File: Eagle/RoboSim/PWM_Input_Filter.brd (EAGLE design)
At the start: 74.6 x 78.7 mm, 68 parts, among them IC1 LM358, IC2 LM358, IC3 LM358

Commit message: updated op amp part number
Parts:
- IC1, IC2, IC3: value LM358 -> TLV2772
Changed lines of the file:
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@@
 </autorouter>
 <elements>
-<element name="IC1" library="SparkFun-AnalogIC" package="DIP08" value="LM358" x="44.45" y="67.31">
+<element name="IC1" library="SparkFun-AnalogIC" package="DIP08" value="TLV2772" x="44.45" y="67.31">
 <attribute name="PROD_ID" value="IC-09172" x="63.5" y="62.23" size="1.778" layer="27" display="off"/>
 </element>
@@
 <element name="JP1" library="SparkFun-Connectors" package="1X06_LOCK" value="" x="5.08" y="59.69" rot="R90"/>
 <element name="JP2" library="SparkFun-Connectors" package="1X06_LOCK" value="" x="69.85" y="44.45" rot="R270"/>
-<element name="IC2" library="SparkFun-AnalogIC" package="DIP08" value="LM358" x="50.8" y="44.45">
+<element name="IC2" library="SparkFun-AnalogIC" package="DIP08" value="TLV2772" x="50.8" y="44.45">
 <attribute name="PROD_ID" value="IC-09172" x="82.55" y="39.37" size="1.778" layer="27" display="off"/>
 </element>
@@
 <element name="TP4" library="SparkFun-Passives" package="PAD.03X.03" value="TEST-POINT3" x="21.59" y="48.26"/>
 <element name="C8" library="SparkFun-Passives" package="CAP-PTH-SMALL" value="100uF" x="59.69" y="39.37" rot="R180"/>
-<element name="IC3" library="SparkFun-AnalogIC" package="DIP08" value="LM358" x="52.07" y="15.24">
+<element name="IC3" library="SparkFun-AnalogIC" package="DIP08" value="TLV2772" x="52.07" y="15.24">
 <attribute name="PROD_ID" value="IC-09172" x="96.52" y="10.16" size="1.778" layer="27" display="off"/>
 </element>

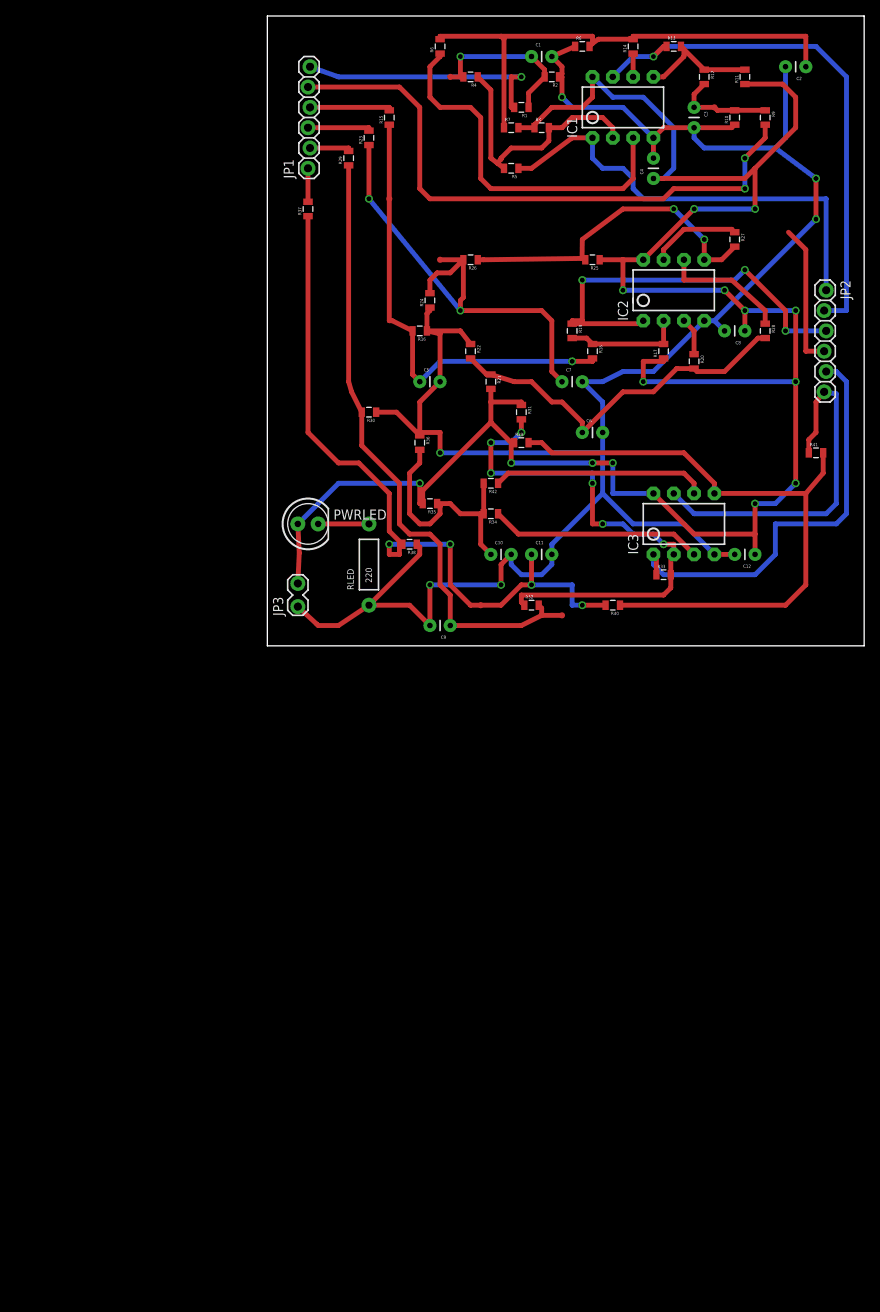
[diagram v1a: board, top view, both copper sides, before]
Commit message: Updated pwm input filter schematic
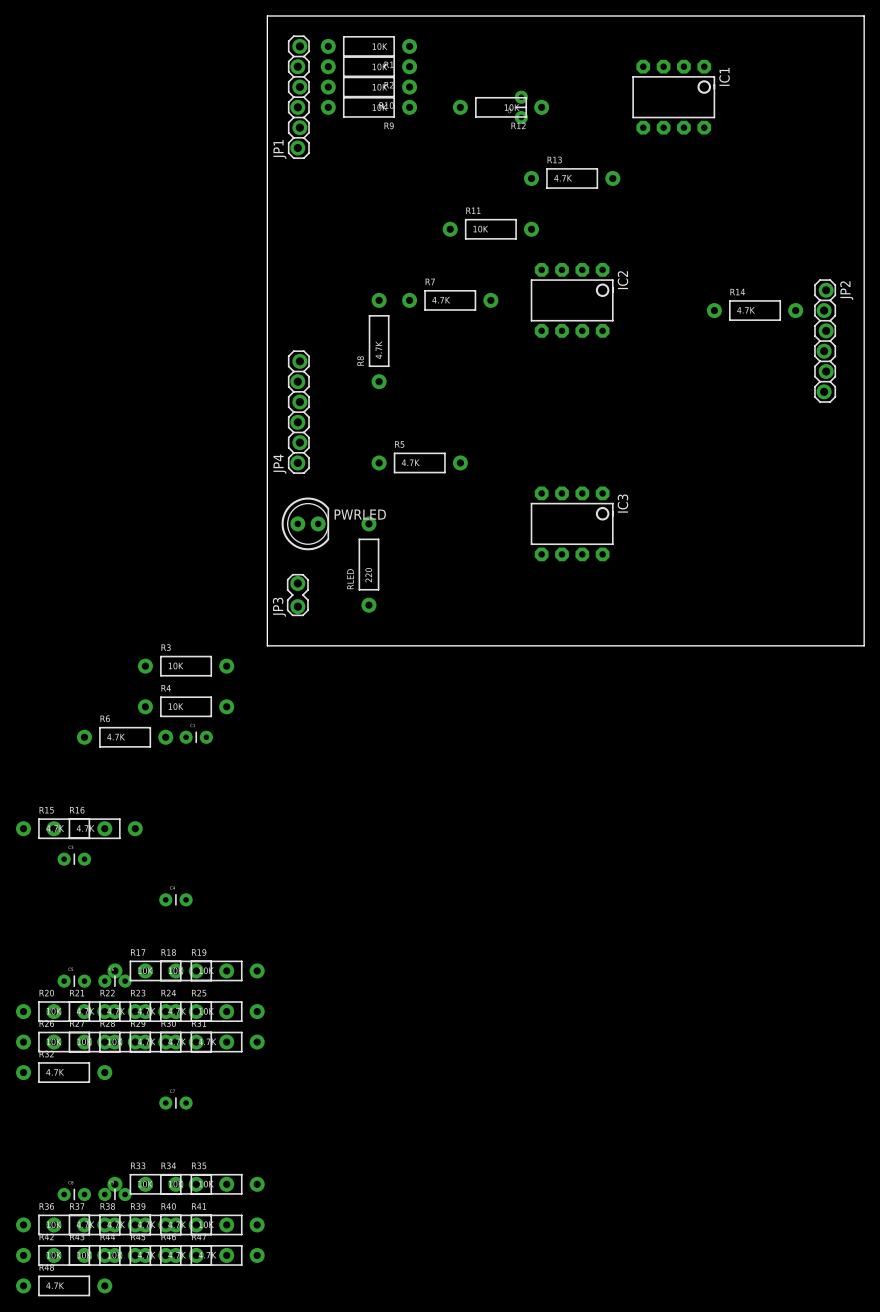
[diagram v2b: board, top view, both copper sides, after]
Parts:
- removed C10, C12: 100uF, SparkFun-Passives:CAP-PTH-SMALL
- removed C11: 0.5uF, SparkFun-Passives:CAP-PTH-SMALL
- removed TP1, TP2, TP3, TP4, TP5, TP6: TEST-POINT3, SparkFun-Passives:PAD.03X.03
- added JP4: (no value), SparkFun-Connectors:1X06_LOCK
- added R43, R44: 10K, SparkFun-Passives:AXIAL-0.4
- added R45, R46, R47, R48: 4.7K, SparkFun-Passives:AXIAL-0.4
- C1, C3, C5, C7, C9: value 0.5uF -> 100uF
- R1, R11, R12, R17, R18, R19, R20, R25, R26, R27, R28, R3, R33, R34, R35, R36, R4, R41, R42, R9: value 80K -> 10K; device SparkFun-Passives:0805 -> SparkFun-Passives:AXIAL-0.4
- R10, R2: value 20K -> 10K; device SparkFun-Passives:0805 -> SparkFun-Passives:AXIAL-0.4
- R13, R14, R15, R21, R22, R23, R29, R31, R32, R37, R39, R40, R5, R6, R7, R8: value 80K -> 4.7K; device SparkFun-Passives:0805 -> SparkFun-Passives:AXIAL-0.4
- R16, R24, R30, R38: value 20K -> 4.7K; device SparkFun-Passives:0805 -> SparkFun-Passives:AXIAL-0.4
- moved C8 137.5 mm to (-25.4, -68.6), turned to 0 degrees
- moved R37 129.8 mm to (-21.6, -72.4), turned to 0 degrees
- moved R27 128.3 mm to (-21.6, -49.5), turned to 0 degrees
- moved C3 122.6 mm to (-25.4, -26.7), turned to 0 degrees
- moved R41 122.2 mm to (-6.35, -72.4)
- moved R28 119.6 mm to (-17.8, -49.5), turned to 0 degrees
- moved R20 113.2 mm to (-25.4, -45.7), turned to 0 degrees
- moved R29 113.1 mm to (-14.0, -49.5), turned to 0 degrees
- moved R23 112.4 mm to (-14.0, -45.7), turned to 0 degrees
- moved R42 110.3 mm to (-25.4, -76.2), turned to 0 degrees
- moved R26 110.2 mm to (-25.4, -49.5), turned to 0 degrees
- moved C4 108.8 mm to (-12.7, -31.8), turned to 0 degrees
- moved R39 107.9 mm to (-14.0, -72.4)
- moved R36 107.4 mm to (-25.4, -72.4), turned to 0 degrees
- moved R25 105.1 mm to (-6.35, -45.7), turned to 0 degrees
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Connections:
- removed net N$4: IC1.1, JP2.1, R5.1
- new net N$18: C6.1, IC2.7, JP2.4, R30.P$2
- new net N$19: JP4.6, R26.P$2
- new net N$23: IC2.3, R17.P$1, R20.P$2, R23.P$2
- new net N$24: R21.P$2, R22.P$1
- new net N$29: R31.P$1, R32.P$2
- new net N$34: JP4.2, R42.P$2
- new net N$35: JP4.1, R41.P$2
- new net N$43: R47.P$1, R48.P$2
- new net N$44: C1.1, IC1.1, JP2.1, R6.P$2
- new net N$6: IC1.2, R1.P$1, R3.P$2, R5.P$1
- net GND: now also R16.P$1, R24.P$1, R32.P$1, R40.P$1, R48.P$1, R8.P$1; no longer C10.2, C11.2, C12.2, R10.1, R16.1, R2.1, R22.1, R24.1, R30.1, R36.1, R38.1, R8.1
- net N$1: now also R1.P$2; no longer R1.2
- net N$10: now also R7.P$1, R8.P$2; no longer IC1.5, R11.2, R12.1, R13.2
- net N$11: now also IC1.5, R10.P$1, R11.P$2, R13.P$1; no longer C2.1, R14.2, R6.2, R7.1, R8.2
- net N$12: now also R12.P$2, R15.P$2, R9.P$1; no longer R14.1
- net N$13: now also C3.1, R14.P$2; no longer R13.1
- net N$14: now also R10.P$2; no longer R15.2
- net N$15: now also R13.P$2, R14.P$1; no longer C5.1, R15.1, R16.2, R18.2, TP3.P$1
- net N$16: now also JP1.1, R17.P$2; no longer IC2.1, JP2.3, R19.1
- net N$17: now also R15.P$1, R16.P$2; no longer IC2.2, R17.2, R18.1, R19.2
- net N$2: now also JP1.2, R18.P$2; no longer C1.1, R1.1, R2.2, R4.2, TP1.P$1
- net N$20: now also JP4.5, R25.P$2; no longer IC2.3, R20.1
- net N$21: now also R9.P$2; no longer R23.2
- net N$22: now also IC2.2, R18.P$1, R19.P$2, R21.P$1; no longer C7.1, R23.1, R24.2, R26.2, TP4.P$1
- net N$25: now also R23.P$1, R24.P$2; no longer IC2.5, R25.2, R26.1, R27.2
- net N$26: now also IC2.5, R26.P$1, R27.P$2, R29.P$1; no longer C6.1, R20.2, R21.1, R22.2, R28.2
- net N$27: now also IC2.6, R25.P$1, R28.P$2, R31.P$2; no longer IC3.1, JP2.5, R33.1
- net N$28: now also R29.P$2, R30.P$1; no longer IC2.6, R28.1
- net N$3: now also C5.1, IC2.1, JP2.3, R22.P$2; no longer IC1.2, R3.2, R4.1, R5.2
- net N$30: now also JP4.4, R34.P$2; no longer IC2.7, JP2.4, R27.1
- net N$31: now also C8.1, IC3.1, JP2.5, R38.P$2; no longer JP1.2, R29.2
- net N$32: now also JP4.3, R33.P$2; no longer C9.1, R29.1, R30.2, R32.2, TP5.P$1
- net N$33: now also C9.1, IC3.7, JP2.6, R46.P$2; no longer IC3.2, R31.2, R32.1, R33.2
- net N$36: now also IC3.2, R34.P$1, R35.P$2, R37.P$1; no longer IC3.3, R34.1
- net N$37: now also IC3.3, R33.P$1, R36.P$2, R39.P$2; no longer JP1.1, R37.2
- net N$38: now also R37.P$2, R38.P$1; no longer C11.1, R37.1, R38.2, R40.2, TP6.P$1
- net N$39: now also R39.P$1, R40.P$2; no longer IC3.5, R39.2, R40.1, R41.2
- net N$40: now also IC3.5, R42.P$1, R43.P$2, R45.P$1; no longer C10.1, R34.2, R35.1, R36.2, R42.2
- net N$41: now also R41.P$1, R44.P$2, R47.P$2; no longer R42.1
- net N$42: now also R45.P$2, R46.P$1; no longer IC3.7, JP2.6, R41.1
- net N$7: now also R2.P$1, R4.P$2, R7.P$2; no longer R6.1
- net N$8: now also R2.P$2; no longer R9.2
- net N$9: now also R5.P$2, R6.P$1; no longer C3.1, R10.2, R12.2, R9.1, TP2.P$1
- net VCC: now also C2.1, C7.1, R11.P$1, R12.P$1, R19.P$1, R20.P$1, R27.P$1, R28.P$1, R3.P$1, R35.P$1, R36.P$1, R4.P$1, R43.P$1, R44.P$1; no longer C12.1, C8.1, R11.1, R17.1, R21.2, R25.1, R3.1, R31.1, R35.2, R39.1, R7.2
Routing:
- net VCC: track 273.1 -> 0.00 mm, vias 14 -> 0
- net GND: track 267.9 -> 0.00 mm, vias 6 -> 0
- net N$38: track 92.1 -> 0.00 mm, vias 4 -> 0
- net N$32: track 79.6 -> 0.00 mm
- net N$39: track 79.6 -> 0.00 mm
- net N$8: track 75.9 -> 0.00 mm, vias 2 -> 0
- net N$13: track 66.5 -> 0.00 mm, vias 1 -> 0
- net N$33: track 66.1 -> 0.00 mm, vias 6 -> 0
- net N$11: track 63.4 -> 0.00 mm
- net N$22: track 61.2 -> 0.00 mm, vias 2 -> 0
- net N$15: track 57.4 -> 0.00 mm, vias 1 -> 0
- net N$4: track 56.6 -> 0.00 mm
- net N$27: track 53.6 -> 0.00 mm
- net N$16: track 51.4 -> 0.00 mm, vias 3 -> 0
- net N$26: track 46.4 -> 0.00 mm
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
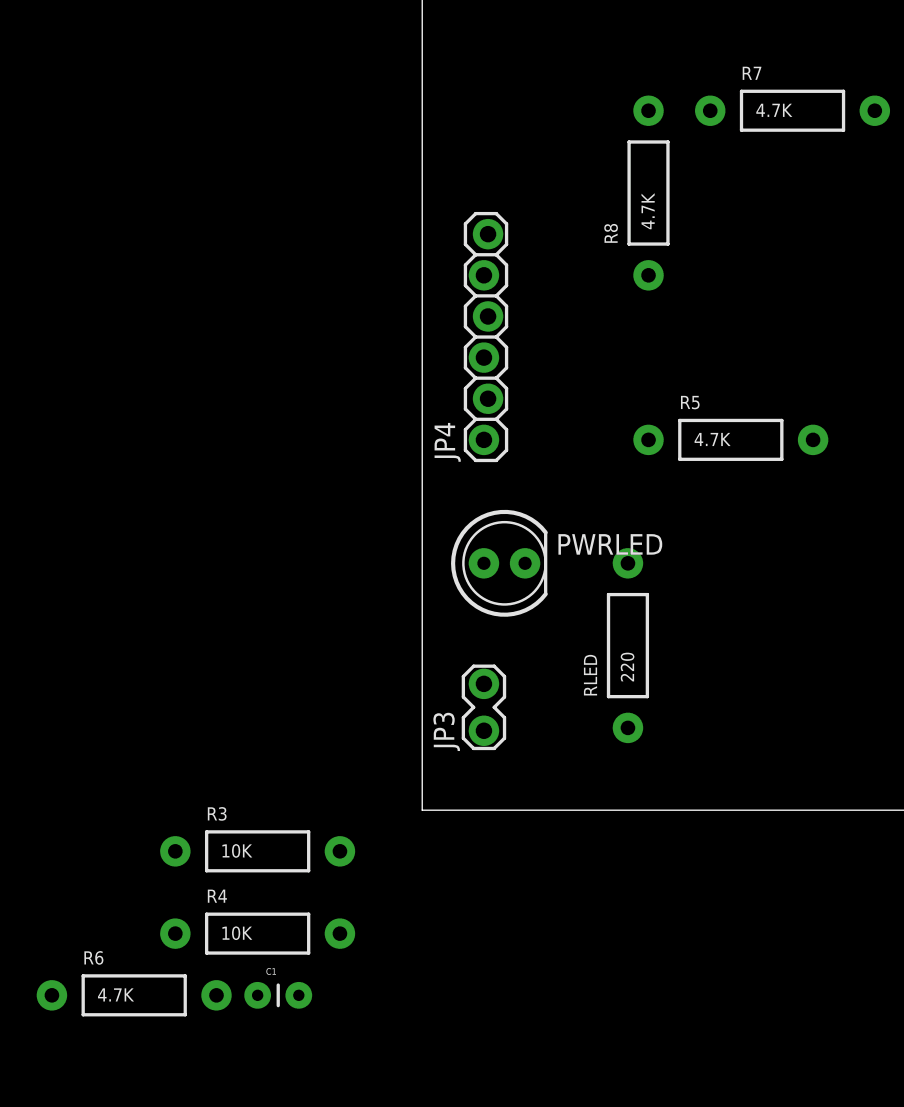
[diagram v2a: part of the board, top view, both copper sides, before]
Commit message: updated circuit 1 on the board to proper experimented values. Need to update the others as well
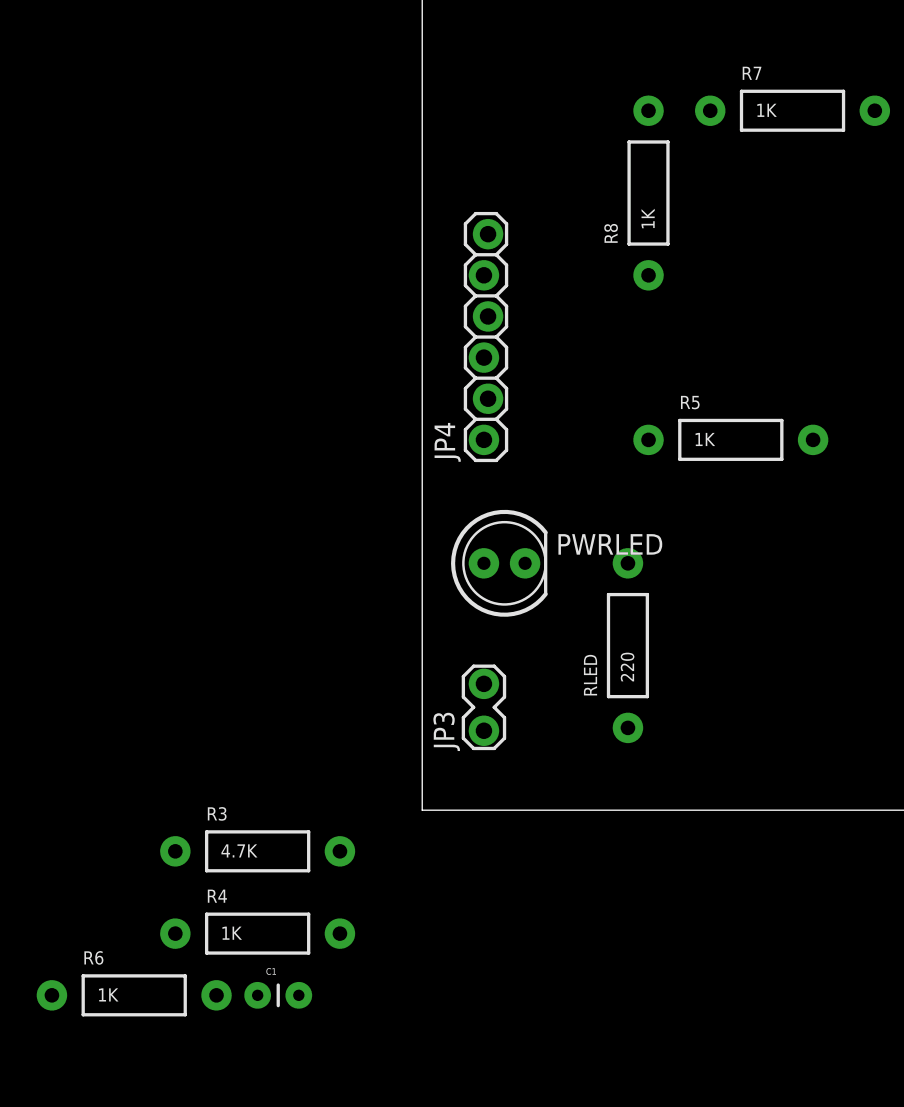
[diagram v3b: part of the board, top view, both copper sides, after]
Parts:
- R3: value 10K -> 4.7K
- R4: value 10K -> 1K
- R5, R6, R7, R8: value 4.7K -> 1K
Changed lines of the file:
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@@
 <?xml version="1.0" encoding="utf-8"?>
 <!DOCTYPE eagle SYSTEM "eagle.dtd">
-<eagle version="6.5.0">
+<eagle version="7.3.0">
 <drawing>
 <settings>
@@
 <pass name="Default">
 <param name="RoutingGrid" value="50mil"/>
+<param name="AutoGrid" value="1"/>
+<param name="Efforts" value="0"/>
+<param name="TopRouterVariant" value="1"/>
 <param name="tpViaShape" value="round"/>
 <param name="PrefDir.1" value="|"/>
@@
 <element name="R2" library="SparkFun-Passives" package="AXIAL-0.4" value="10K" x="12.7" y="72.39" rot="R180"/>
 <element name="R1" library="SparkFun-Passives" package="AXIAL-0.4" value="10K" x="12.7" y="74.93" rot="R180"/>
-<element name="R3" library="SparkFun-Passives" package="AXIAL-0.4" value="10K" x="-10.16" y="-2.54"/>
-<element name="R4" library="SparkFun-Passives" package="AXIAL-0.4" value="10K" x="-10.16" y="-7.62"/>
+<element name="R3" library="SparkFun-Passives" package="AXIAL-0.4" value="4.7K" x="-10.16" y="-2.54"/>
+<element name="R4" library="SparkFun-Passives" package="AXIAL-0.4" value="1K" x="-10.16" y="-7.62"/>
 <element name="C1" library="SparkFun-Passives" package="CAP-PTH-SMALL" value="100uF" x="-10.16" y="-11.43"/>
-<element name="R5" library="SparkFun-Passives" package="AXIAL-0.4" value="4.7K" x="19.05" y="22.86"/>
-<element name="R6" library="SparkFun-Passives" package="AXIAL-0.4" value="4.7K" x="-17.78" y="-11.43"/>
-<element name="R7" library="SparkFun-Passives" package="AXIAL-0.4" value="4.7K" x="22.86" y="43.18"/>
-<element name="R8" library="SparkFun-Passives" package="AXIAL-0.4" value="4.7K" x="13.97" y="38.1" rot="R90"/>
+<element name="R5" library="SparkFun-Passives" package="AXIAL-0.4" value="1K" x="19.05" y="22.86"/>
+<element name="R6" library="SparkFun-Passives" package="AXIAL-0.4" value="1K" x="-17.78" y="-11.43"/>
+<element name="R7" library="SparkFun-Passives" package="AXIAL-0.4" value="1K" x="22.86" y="43.18"/>
+<element name="R8" library="SparkFun-Passives" package="AXIAL-0.4" value="1K" x="13.97" y="38.1" rot="R90"/>
 <element name="R9" library="SparkFun-Passives" package="AXIAL-0.4" value="10K" x="12.7" y="67.31" rot="R180"/>
 <element name="R10" library="SparkFun-Passives" package="AXIAL-0.4" value="10K" x="12.7" y="69.85" rot="R180"/>
